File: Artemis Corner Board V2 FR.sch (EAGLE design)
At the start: 59 parts, among them U1 TPS562219, U2 TM4C1231C3PM, U21 LM1085IS, U3 TPS562219, U4 MCP2562FD

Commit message: Added Series Termination Resistors
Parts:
- added C25, C26: 12pF, rcl:C-USC0805
- added J1: (no value), FormE:CTI-20-MALE
- added R13: 1K, rcl:R-US_R0805
- added R14, R16, R17, R19: 22, rcl:R-US_R0805
- added Y1: NX3225GA, FormE:NX3225GA
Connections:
- removed net IR_SENSOR_1_ANALOG_OUT: H1.30, U2.PD0/AIN7/I2C3SCL/SSI1CLK/SSI3CLK/WT2CCP0
- removed net IR_SENSOR_1_DIGITAL_IN: H1.19, U2.PC2/T5CCP0/TDI
- removed net IR_SENSOR_1_DIGITAL_OUT: H1.15, U2.PC3/SWO/T5CCP1/TDO
- removed net IR_SENSOR_2_ANALOG_OUT: H1.29, U2.PD1/AIN6/I2C3SDA/SSI1FSS/SSI3FSS/WT2CCP1
- removed net IR_SENSOR_2_DIGITAL_IN: H1.18, U2.PC1/SWDIO/T4CCP1/TMS
- removed net IR_SENSOR_2_DIGITAL_OUT: H1.14, U2.PB3/I2C0SDA/T3CCP1
- removed net IR_SENSOR_3_ANALOG_OUT: H1.28, U2.PD2/AIN5/SSI1RX/SSI3RX/WT3CCP0
- removed net IR_SENSOR_3_DIGITAL_IN: H1.17, U2.PC0/SWCLK/T4CCP0/TCK
- removed net IR_SENSOR_3_DIGITAL_OUT: H1.13, U2.PB2/I2C0SCL/T3CCP0
- new net DAMPER_POS_OUT_TR: R16.2, U2.PA0/U0RX
- new net N$5: C25.1, U2.OSC1, Y1.P$1
- new net N$6: C26.1, U2.OSC0, Y1.P$3
- new net STRAIN_GADGE_VOLTMETER_IN_0_TR: R17.2, U2.PE3/AIN0
- new net STRAIN_GADGE_VOLTMETER_IN_1_TR: R19.2, U2.PE2/AIN1
- new net TCK: J1.11, R13.1, U2.PC0/SWCLK/T4CCP0/TCK
- new net TDI: J1.3
- new net TDO: J1.7, U2.PC2/T5CCP0/TDI, U2.PC3/SWO/T5CCP1/TDO
- new net TMS: J1.1, U2.PC1/SWDIO/T4CCP1/TMS
- new net TRCLK: U2.PF3/CAN0TX/SSI1FSS/T1CCP1/TRCLK
- new net WHEEL_SPEED_OUT_TR: R14.2, U2.PA4/SSI0RX
- net +12V: no longer H1.4, H1.5, H1.6
- net +3V3: now also J1.5
- net +5V: now also H1.10
- net DAMPER_POS_OUT: now also R16.1; no longer U2.PA0/U0RX
- net GND: now also C25.2, C26.2, H1.19, J1.10, J1.12, J1.16, J1.20, J1.4, J1.8, R13.2
- net MCU_RESET: now also J1.15
- net PROGRAMMING_CAN_N: now also H1.12
- net PROGRAMMING_CAN_P: now also H1.11
- net STRAIN_GADGE_VOLTMETER_IN_0: now also H1.28, R17.1; no longer H1.27, U2.PE3/AIN0
- net STRAIN_GADGE_VOLTMETER_IN_1: now also R19.1; no longer U2.PE2/AIN1
- net WHEEL_SPEED_OUT: now also R14.1; no longer U2.PA4/SSI0RX
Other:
- note added: "+5V to Image Sensor Board"
- note added: "Key"
- note added: "Manual Reset Button And JTAG Connector"
- note removed: "Manual Reset Button"

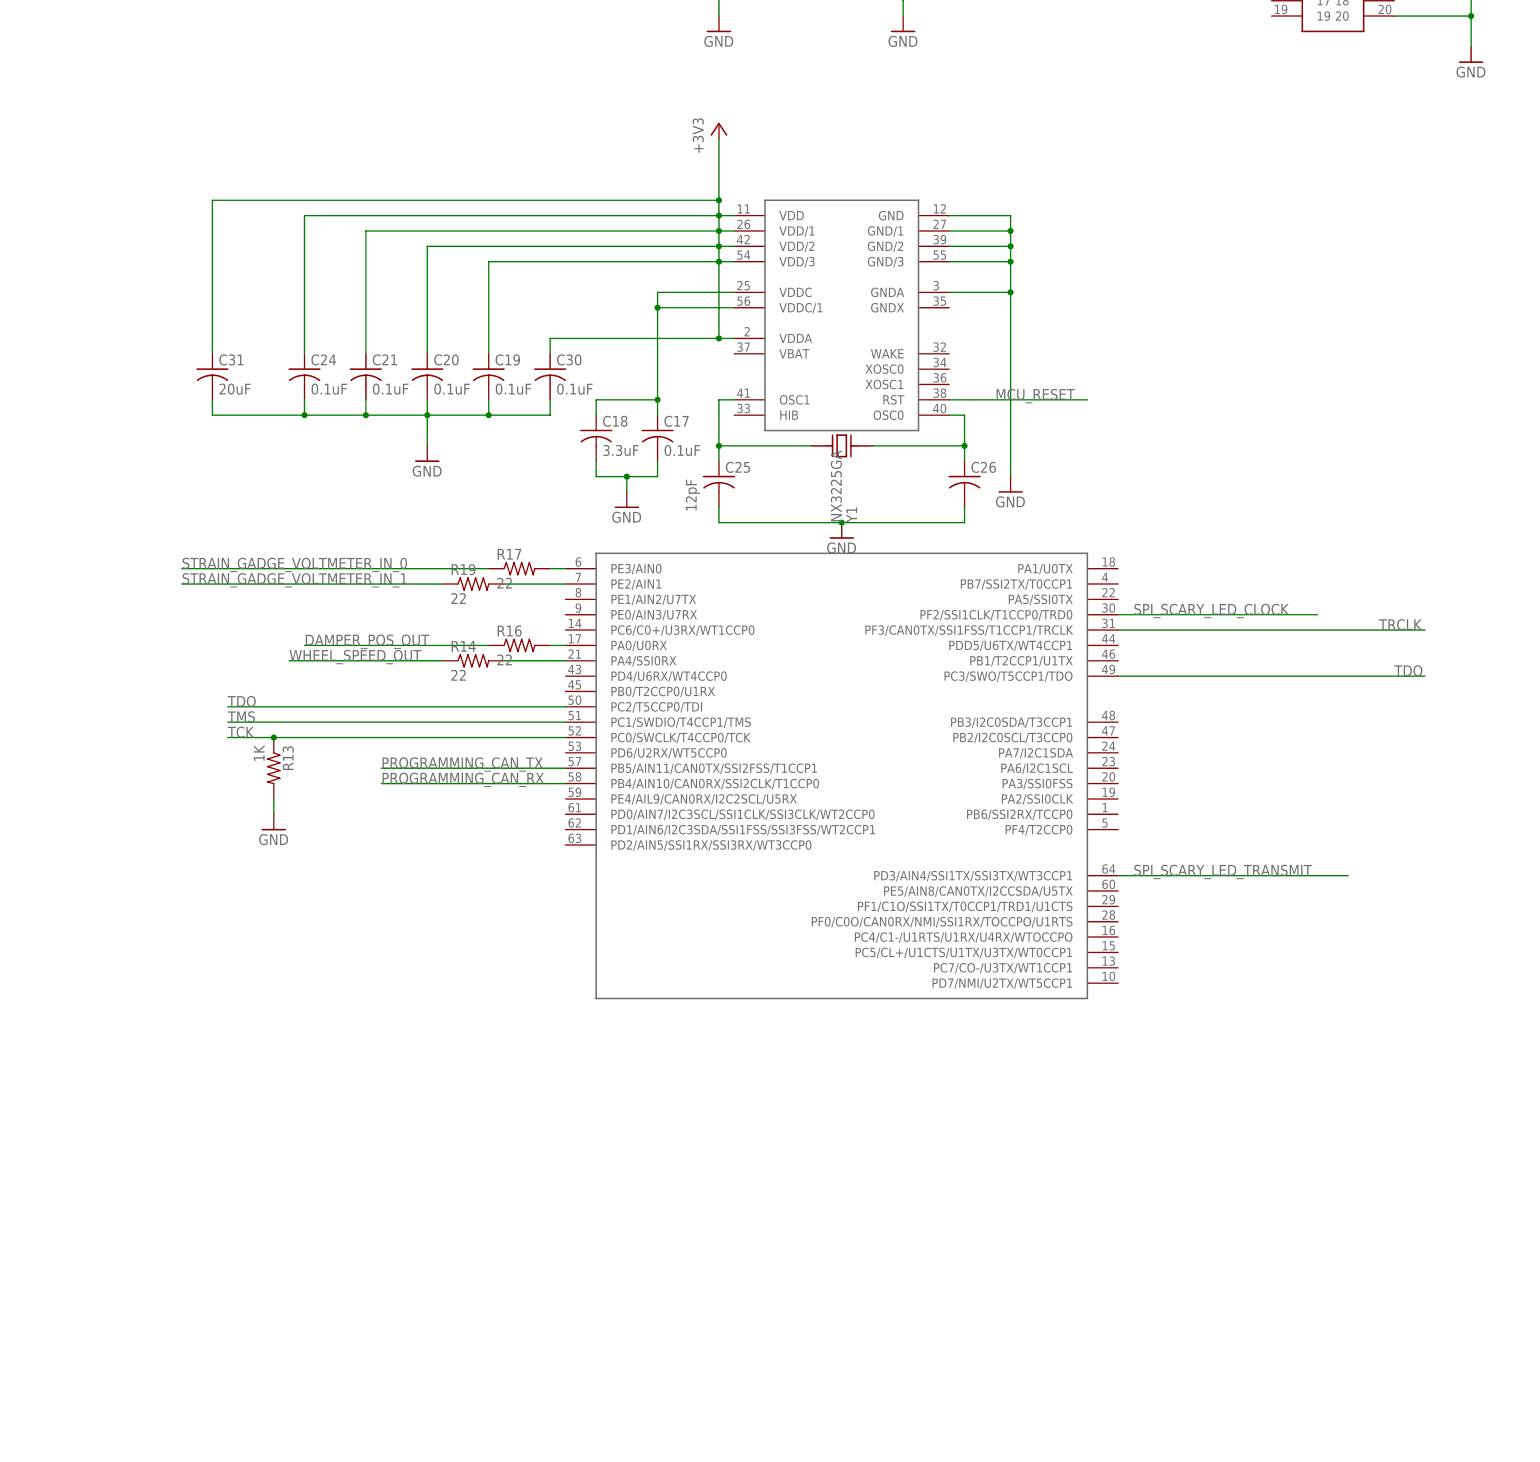
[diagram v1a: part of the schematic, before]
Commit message: fixed board errors and added ESD Protection
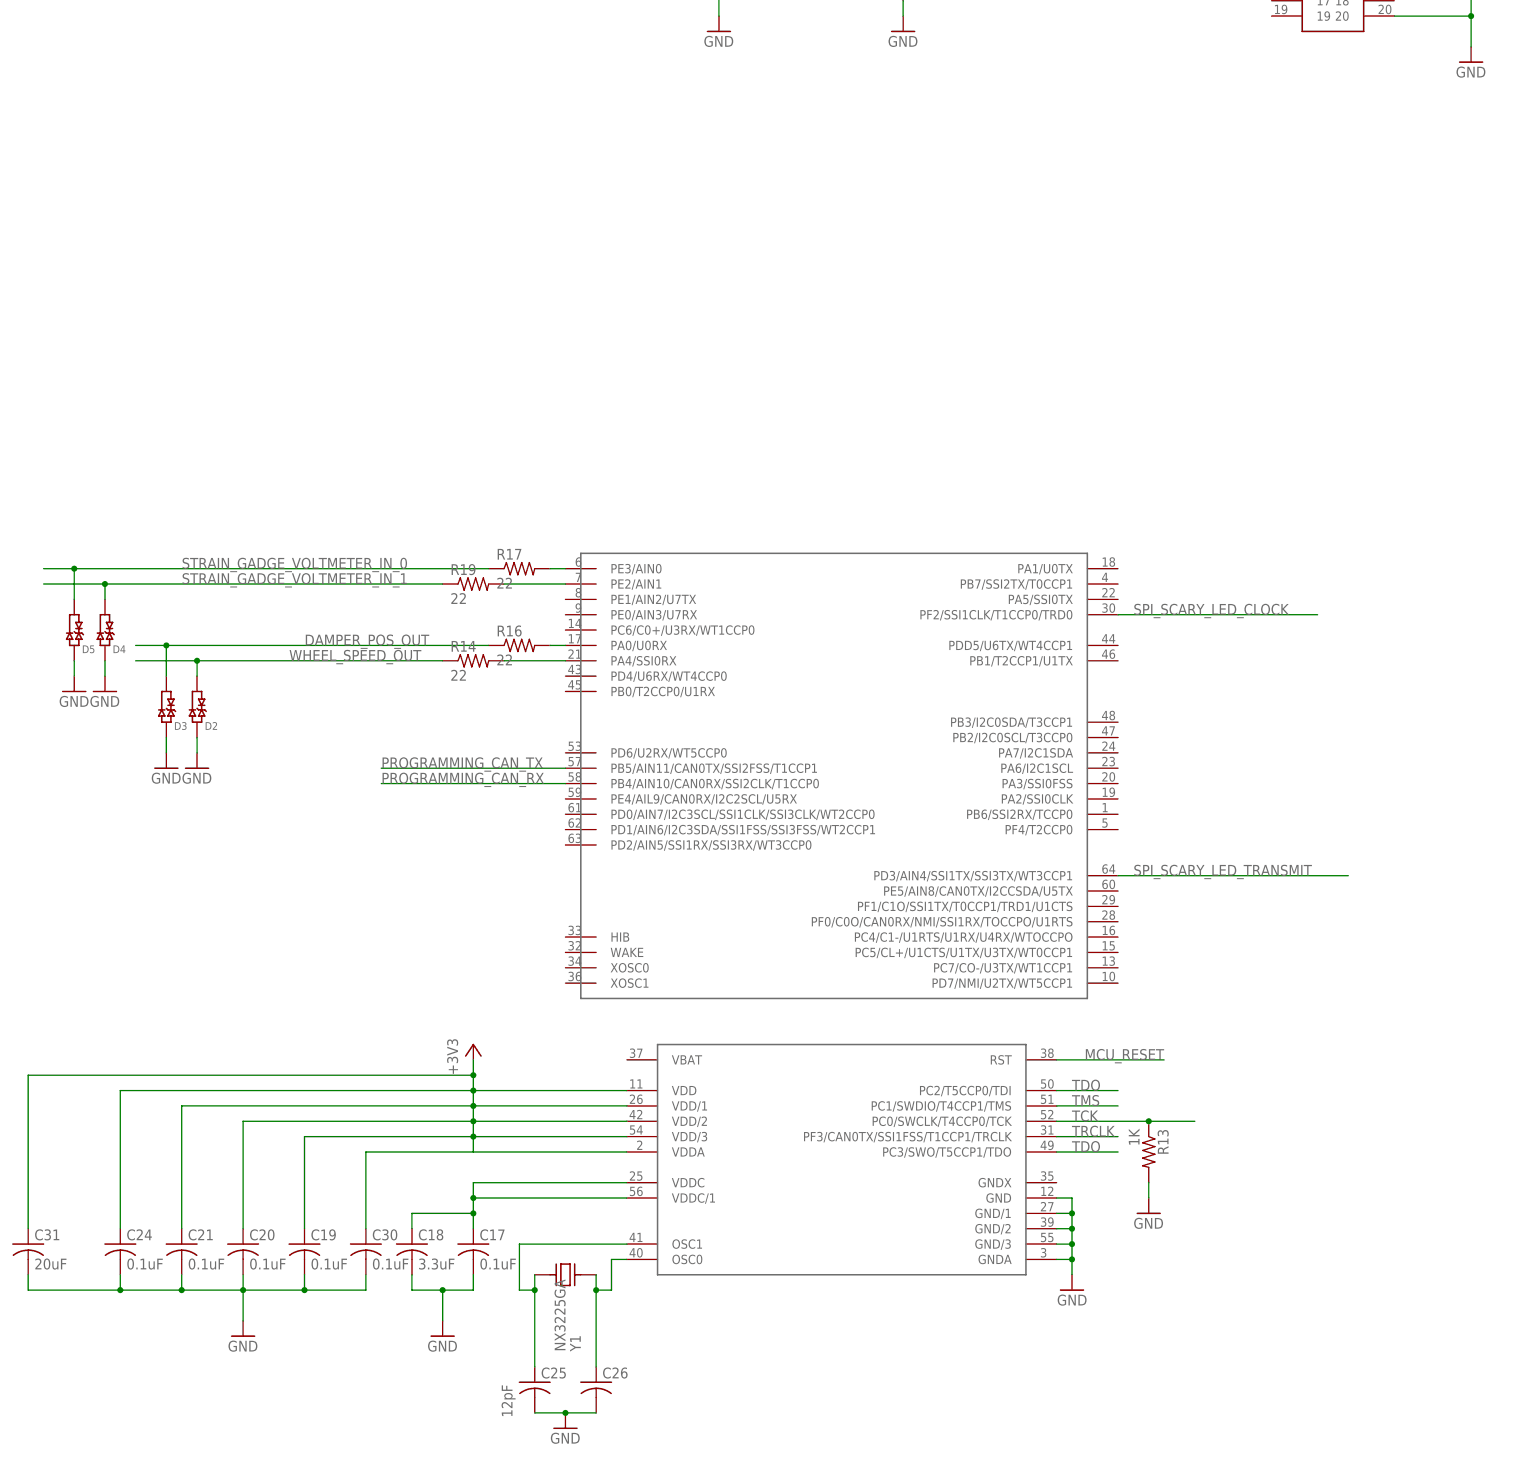
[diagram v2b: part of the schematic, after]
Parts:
- added D2, D3, D4, D5: TPD1E05U06, FormE:TPD1E05U06
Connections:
- net DAMPER_POS_OUT: now also D3.I/O
- net GND: now also D2.P$2, D3.P$2, D4.P$2, D5.P$2
- net STRAIN_GADGE_VOLTMETER_IN_0: now also D5.I/O
- net STRAIN_GADGE_VOLTMETER_IN_1: now also D4.I/O
- net WHEEL_SPEED_OUT: now also D2.I/O
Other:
- moved on the sheet: C17, C18, C19, C20, C21, C24, C25, C26, C30, C31, R13, Y1

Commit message: Made list fixes
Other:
- moved on the sheet: C1, C10, C11, C12, C13, C14, C15, C16, C17, C18, C19, C2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

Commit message: Updated a lot of stuff
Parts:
- added C62: 4.7uF, rcl:C-USC0805
- added C63: 0.1uF, rcl:C-USC0805
- added FB3: 220R @ 100M, launchpad:INDUCTOR
- added R20: 2K, rcl:R-US_R0805
- C31: value 20uF -> 22uF
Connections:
- net P$40 renamed VDDC
- net PROGRAMMING_CAN_N renamed CAN_N
- net PROGRAMMING_CAN_P renamed CAN_P
- net PROGRAMMING_CAN_RX renamed CAN_RX
- net PROGRAMMING_CAN_TX renamed CAN_TX
- new net FILTERED_+3V3: C19.1, C20.1, C21.1, C24.1, C30.1, C31.1, C62.1, C63.1, FB3.2, U2.VDD, U2.VDD/1, U2.VDD/2, U2.VDD/3, U2.VDDA
- new net N$7: R20.2, U2.OSC1
- net +3V3: now also FB3.1; no longer C19.1, C20.1, C21.1, C24.1, C30.1, C31.1, U2.VDD, U2.VDD/1, U2.VDD/2, U2.VDD/3, U2.VDDA
- net GND: now also C62.2, C63.2, U2.GNDX, U2.WAKE
- net N$5: now also R20.1; no longer U2.OSC1
- net TDI: now also U2.PC2/T5CCP0/TDI
- net TDO: no longer U2.PC2/T5CCP0/TDI
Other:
- moved on the sheet: C25, C26, Y1

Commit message: Changed to Tiva C with two CAN modules; modified sensor input scaling
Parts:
- removed C62: 4.7uF, rcl:C-USC0805
- removed C63: 0.1uF, rcl:C-USC0805
- removed C72, C73: 10uF, adafruit:C-USC0805
- removed D4, D5: TPD1E05U06, FormE:TPD1E05U06
- removed FB3: 220R @ 100M, launchpad:INDUCTOR
- removed LED5, LED6: GREEN, FormE:LEDCHIPLED_0805
- removed LED7: APA102C, FormE:APA102C
- removed S2: TE-FSM4JSMATR, FormE:TE-FSM4JSMATR
- removed U21: LM1085IS, FormE:LM1085
- added C27, C33, C34, C35: 0.1uF, rcl:C-USC0805
- added C28: 0.01uF, rcl:C-USC0805
- added C29: 1uF, rcl:C-USC0805
- added C32: 4.7uF, rcl:C-USC0805
- added C36, C42: 0.1uF, adafruit:C-USC0805
- added C37, C38: 10uF, adafruit:C-USC0805
- added C40: 2.2uF, rcl:C-USC0805
- added C41: 8200pF, adafruit:C-USC0805
- added C43, C44: 22uF, rcl:C-USC1210K
- added C45, C46, C47: 22uF, adafruit:C-USC0805
- added CF1, CF2, CF3, CF4: NFM21C, murata-filter:NFM21C
- added D1: TPD1E05U06, FormE:TPD1E05U06
- added IC1: FT232RL, ftdichip:FT232RL
- added JP1: (no value), pinhead:PINHD-1X2
- added JP2: (no value), FormE:USB_MICROB_PLUG-PTH3
- added L3: 4.7uH, FormE:SRP6540
- added Q1: BSS138, FormE:BSS138
- added R21: 1k, adafruit:R-US_R0805
- added R22: 54.9k, adafruit:R-US_R0805
- added R23: 10K, adafruit:R-US_R0805
- added R24: 1K, adafruit:R-US_R0805
- added S1: TE-FSM4JSMATR, FormE:TE-FSM4JSMATR
- added U5: MCP2562, FormE:MCP256X-SOIC
- added U6: TPS62177, FormE:TPS6217X
- added U7: TPS62175, FormE:TPS6217X
- added U8: TPS562219, FormE:TPS562219
- added Y2: 32.768kHz, FormE:AB26TRQ
- C1: value 0.1uF -> 100uF; device adafruit:C-USC0805 -> rcl:CPOL-USD/7343-31W; PARTNO GRM21BR71E104KA01L -> T494D107K010AT
- C10, C2: value 10uF -> 0.1uF; device adafruit:C-USC0805 -> rcl:C-USC0805; PARTNO GRM21BR61E106KA73L -> *
- C11: value 10uF -> 2.2uF; device adafruit:C-USC0805 -> rcl:C-USC0805; PARTNO GRM21BR61E106KA73L -> *
- C12: value 8200pF -> 2.2uF; device adafruit:C-USC0805 -> rcl:C-USC0805; PARTNO C0805C822K5RACTU -> *
- C13, C5: device adafruit:C-USC0805 -> rcl:C-USC0805
- C14, C16: value 22uF -> 0.1uF; device adafruit:C-USC0805 -> rcl:C-USC0805; PARTNO C2012JB1E226M125AC -> GRM21BR71E104KA01L
- C15: value 22uF -> DNP/0.1uF; device adafruit:C-USC0805 -> rcl:C-USC0805; PARTNO C2012JB1E226M125AC -> *
- C17, C30: PARTNO (none) -> GRM21BR71E104KA01L
- C18: value 3.3uF -> 22pF; PARTNO (none) -> C0805C220K5GACTU
- C19: value 0.1uF -> 1uF; PARTNO (none) -> *
- C20: value 0.1uF -> 22pF; PARTNO (none) -> C0805C220K5GACTU
- C21: value 0.1uF -> 2.2uF; PARTNO (none) -> *
- C22, C23: value 0.1uF -> 22pF; PARTNO GRM21BR71H104KA01L -> C0805C220K5GACTU
- C24: value 0.1uF -> 0.01uF; PARTNO (none) -> *
- C25: value 12pF -> 0.1uF; MPN 08051A150JAT2A -> (none); OC_NEWARK 96M1322 -> (none); PARTNO CL21C150JBANNNC -> GRM21BR71E104KA01L
- C26: value 12pF -> 0.01uF; MPN 08051A150JAT2A -> (none); OC_NEWARK 96M1322 -> (none); PARTNO CL21C150JBANNNC -> *
- C3: value 10uF -> 100pF; device adafruit:C-USC0805 -> rcl:C-USC0805; PARTNO GRM21BR61E106KA73L -> *
- C31: value 22uF -> 0.1uF; PARTNO (none) -> GRM21BR71E104KA01L
- C39: value 1uF -> 2.2uF; PARTNO EMK212B7105KG-T -> UMK212BB7225KG-T
- C4: value 8200pF -> 100pF; device adafruit:C-USC0805 -> rcl:C-USC0805; PARTNO C0805C822K5RACTU -> *
- C6, C7, C8: value 22uF -> 2.2uF; device adafruit:C-USC0805 -> rcl:C-USC0805; PARTNO C2012JB1E226M125AC -> *
- C9: value 0.1uF -> DNP; device adafruit:C-USC0805 -> rcl:C-USC0805; PARTNO GRM21BR71E104KA01L -> *
- D3: value TPD1E05U06 -> MM3Z3V3T1G; device FormE:TPD1E05U06 -> FormE:MM3Z3V3T1G; PARTNO (none) -> MM3Z3V3T1G
- L1, L2: value 4.7uH -> 10uH; PARTNO SRP6540-4R7M -> SRP6540-100M
- LED1, LED2: value APA102C -> ORANGE; device FormE:APA102C -> FormE:LEDCHIP-LED0805; PARTNO (none) -> 598-8130-107F
- LED3: device FormE:LEDCHIPLED_0805 -> FormE:LEDCHIP-LED0805
- LED4: value APA102C -> GREEN; device FormE:APA102C -> FormE:LEDCHIP-LED0805; PARTNO (none) -> 598-8170-107F
- R1: value 33.2K -> 100R; device adafruit:R-US_R0805 -> rcl:R-US_R0805; PARTNO ERA-6AEB5492V -> (none)
- R10: value 10K -> 270; device adafruit:R-US_R0805 -> rcl:R-US_R0805; PARTNO ERJ-6ENF1002V -> ERJ-6ENF2700V
- R11: value 100 -> 120R; PARTNO ERJ-6ENF1000V -> ERJ-6ENF1200V
- R12: value 2.2K -> 100R; PARTNO ERA-6AEB222V -> *
- R13: value 1K -> 10k; PARTNO ERA-6AEB222V -> *
- R14: value 22 -> 120R; PARTNO ERA-6AEB222V -> ERJ-6ENF1200V
- R15: value 0.007 -> 270; device adafruit:R-US_R0805 -> rcl:R-US_R0805; PARTNO PMR10EZPFU7L00 -> ERJ-6ENF2700V
- R16: value 22 -> 270; PARTNO ERA-6AEB222V -> ERJ-6ENF2700V
- R17: value 22 -> 10k; PARTNO ERA-6AEB222V -> ERJ-6ENF1002V
- R18: value 1K -> 4.7k; device adafruit:R-US_R0805 -> rcl:R-US_R0805; PARTNO ERJ-6ENF1001V -> ERJ-6ENF4701V
- R19: value 22 -> 75k; PARTNO ERA-6AEB222V -> ERJ-6ENF7502V
- R2: value 10K -> 100R; device adafruit:R-US_R0805 -> rcl:R-US_R0805; PARTNO ERJ-6ENF1002V -> (none)
- R20: value 2K -> 150k; PARTNO ERA-6AEB222V -> ERJ-6ENF1503V
- R3: value 10K -> 22; device adafruit:R-US_R0805 -> rcl:R-US_R0805; PARTNO ERJ-6ENF1002V -> *
- R4: value 1K -> 22; device adafruit:R-US_R0805 -> rcl:R-US_R0805; PARTNO ERJ-6ENF1001V -> *
- R5: value 33.2K -> 10k; device adafruit:R-US_R0805 -> rcl:R-US_R0805; PARTNO ERA-6AEB5492V -> ERJ-6ENF1002V
- R6: value 10K -> 10k; device adafruit:R-US_R0805 -> rcl:R-US_R0805
- R7: value 120/DNP -> 10k; PARTNO * -> ERJ-6ENF1002V
- R8: value 10K -> 39k; device adafruit:R-US_R0805 -> rcl:R-US_R0805; PARTNO ERJ-6ENF1002V -> ERJ-6ENF3902V
- R9: value 1K -> 75k; device adafruit:R-US_R0805 -> rcl:R-US_R0805; PARTNO ERJ-6ENF1001V -> ERJ-6ENF7502V
- U1: value TPS562219 -> OPA365AIDBVR; device FormE:TPS562219 -> FormE:OPA365AIDBV; PARTNO TPS562219DDFT -> (none)
- U2: value TM4C1231C3PM -> ADS1232IPWR; device FormE:TM4C1231C3PM -> FormE:ADS1232IPWR
- U3: value TPS562219 -> MCP2562; device FormE:TPS562219 -> FormE:MCP256X-SOIC; PARTNO TPS562219DDFT -> MCP2562FD-E/SN
- U4: value MCP2562FD -> TM4C123GH6PMI; device FormE:MCP256X-SOIC -> FormE:TM4C123GH6PM; PARTNO MCP2562FD-E/SN -> (none)
- Y1: value NX3225GA -> 16MHz; device FormE:NX3225GA -> FormE:CSM-3X; PARTNO (none) -> ECS-160-20-3X-TR
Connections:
- removed net +12V: H1.1, H1.2, H1.3, LED6.A, R10.2, R15.2
- removed net 12V_CURRENT_SENSE+: C73.1, R15.1, U21.OUT
- removed net CAN_N: H1.12, H1.35, R7.1, U4.CANL
- removed net CAN_P: H1.11, H1.34, R7.2, U4.CANH
- removed net CAN_RX: U2.PB4/AIN10/CAN0RX/SSI2CLK/T1CCP0, U4.RXD
- removed net CAN_TX: U2.PB5/AIN11/CAN0TX/SSI2FSS/T1CCP1, U4.TXD
- removed net DAMPER_POS_OUT: D3.I/O, H1.25, R16.1
- removed net DAMPER_POS_OUT_TR: R16.2, U2.PA0/U0RX
- removed net FILTERED_+3V3: C19.1, C20.1, C21.1, C24.1, C30.1, C31.1, C62.1, C63.1, FB3.2, U2.VDD, U2.VDD/1, U2.VDD/2, U2.VDD/3, U2.VDDA
- removed net MCU_RESET: C39.1, J1.15, R11.1, R12.2, U2.RST
- removed net N$11: LED6.C, R18.2
- removed net SPI_SCARY_LED_CLOCK: LED1.CI, U2.PF2/SSI1CLK/T1CCP0/TRD0
- removed net SPI_SCARY_LED_TRANSMIT: LED1.DI, U2.PD3/AIN4/SSI1TX/SSI3TX/WT3CCP1
- removed net SS_5V1: C4.1, U1.SS
- removed net SS_5V2: C12.1, U3.SS
- removed net STRAIN_GADGE_VOLTMETER_IN_0: D5.I/O, H1.28, R17.1
- removed net STRAIN_GADGE_VOLTMETER_IN_0_TR: R17.2, U2.PE3/AIN0
- removed net STRAIN_GADGE_VOLTMETER_IN_1: D4.I/O, H1.26, R19.1
- removed net STRAIN_GADGE_VOLTMETER_IN_1_TR: R19.2, U2.PE2/AIN1
- removed net SW_5V1: C5.2, L1.P$1, U1.SW
- removed net SW_5V2: C13.2, L2.P$1, U3.SW
- removed net TRCLK: U2.PF3/CAN0TX/SSI1FSS/T1CCP1/TRCLK
- removed net VBST_5V1: C5.1, U1.VBST
- removed net VBST_5V2: C13.1, U3.VBST
- removed net VDDC: C17.1, C18.1, U2.VDDC, U2.VDDC/1
- removed net VFB_5V1: R1.1, R2.2, U1.VFB
- removed net VFB_5V2: R5.1, R6.2, U3.VFB
- removed net WHEEL_SPEED_OUT: D2.I/O, H1.24, R10.1, R14.1
- removed net WHEEL_SPEED_OUT_TR: R14.2, U2.PA4/SSI0RX
- new net !RESET!: C15.1, J1.15, R12.2, R13.2, U4P.!RST!
- new net +1V2: C44.1, L2.P$2, R19.2, U7.SLEEP, U7.VOS
- new net ADC_!PWDN!: U2.!PDWN!, U4IO.PB1/T2CCP1/U1TX/USB0VBUS
- new net ADC_CHANNEL_SELECT: U2.A0, U4IO.PB3/I2C0SDA/T3CCP1
- new net ADC_GAIN_BIT_0: U2.GAIN0, U4IO.PB4/AIN10/CAN0RX/M0PWM2/SSI2CLK/T1CCP0
- new net ADC_GAIN_BIT_1: U2.GAIN1, U4IO.PB5/AIN11/CAN0TX/M0PWM3/SSI2FSS/T1CCP1
- new net ADC_MISO: U2.!DRDY!/DOUT, U4IO.PA4/SSI0RX
- new net ADC_SCLK: U2.SCLK, U4IO.PA2/SSI0CLK
- new net ADC_SPEED: U2.SPEED, U4IO.PB0/T2CCP0/U1RX/USB0ID
- new net ADC_TEMP_EN: U2.TEMP, U4IO.PB2/I2C0SCL/T3CCP0
- new net CAR_CAN_N: H1.35, R14.1, U5.CANL
- new net CAR_CAN_P: H1.34, R14.2, U5.CANH
- new net CAR_CAN_RX: U4IO.PE4/AIN9/CAN0RX/I2C2SCL/M0PWM4/M1PWM2/U5RX, U5.RXD
- new net CAR_CAN_TX: U4IO.PE5/AIN8/CAN0TX/I2C2SDA/M0PWM5/M1PWM3/U5TX, U5.TXD
- new net DAMPER_POSITION: D1.I/O, H1.25, R3.1
- new net DAMPER_POSITION_3V3: D3.CATHODE, R10.2, U4IO.PE3/AIN0
- new net FB_1V2: R19.1, R20.2, U7.FB
- new net IR_SENSOR_CAN_N: H1.12, R11.1, U3.CANL
- new net IR_SENSOR_CAN_P: H1.11, R11.2, U3.CANH
- new net N$14: R8.2, U1.INVERTING, U1.OUT
- new net N$17: C23.1, U4P.XOSC0, Y2.P$1
- new net N$19: JP1.2, U2.AINP2
- new net N$20: R3.2, R5.1, U1.NONINVERTING
- new net N$21: Q1.D, R4.2, R6.1
- new net N$22: C35.1, IC1.3V3OUT
- new net N$23: JP2.VCC, R18.1
- new net N$24: C22.2, C23.2, U4P.GNDX
- new net N$27: C2.1, C3.1, CF1.3, U2.AINP1
- new net N$29: C2.2, C4.1, CF2.1, U2.AINN1
- new net N$41: IC1.CBUS1, R16.1
- new net N$42: IC1.CBUS0, R15.1
- new net N$45: LED1.C, R15.2
- new net N$46: LED2.C, R16.2
- new net N$52: IC1.!RESET, R17.1, R18.2
- new net N$8: C10.2, U2.CAP1
- new net NTRST: J1.2
- new net PGOOD: U6.PG, U7.PG, U8.PGOOD
- new net RTCK: J1.9
- new net SENSOR_CAN_RX: U3.RXD, U4IO.PA0/CAN1RX/U0RX
- new net SENSOR_CAN_TX: U3.TXD, U4IO.PA1/CAN1TX/U0TX
- new net SS_5V: C41.1, U8.SS
- new net STRAIN_GAUGE_NEGATIVE: CF2.3, H1.26
- new net STRAIN_GAUGE_POSITIVE: CF1.1, H1.28
- new net SW_1V2: L2.P$1, U7.SW
- new net SW_3V3: L1.P$1, U6.SW
- new net SW_5V: C42.2, L3.P$1, U8.SW
- new net UART_RX: IC1.TXD, U4IO.PC4/C1-/IDX1/M0PWM6/U1RTS/U1RX/U4RX/WT0CCP0
- new net UART_TX: IC1.RXD, U4IO.PC5/C1+/M0PWM7/PHA1/U1CTS/U1TX/U4TX/WT0CCP1
- new net USB_D_N: IC1.USBDM, JP2.D-
- new net USB_D_P: IC1.USBDP, JP2.D+
- new net VBST_5V: C42.1, U8.VBST
- new net VFB_5V: R22.1, R23.2, U8.VFB
- new net WHEEL_TACHOMETER: D2.I/O, H1.24, R4.1
- new net WHEEL_TACHOMETER_3V3: Q1.S, R7.1, U4IO.PB6/M0PWM0/SSI2RX/T0CCP0
- net +3V3: now also C12.1, C13.1, C24.1, C25.1, C26.1, C27.1, C28.1, C29.1, C31.1, C34.1, C43.1, IC1.VCCIO, LED1.A, LED2.A, LED3.A, Q1.G, R13.1, R7.2, U2.DVDD, U3.SPLIT/VIO, U4P.VBAT, U4P.VDD, U4P.VDDA, U5.SPLIT/VIO, U6.SLEEP, U6.VOS; no longer C23.1, C6.1, C7.1, C8.1, FB3.1, LED5.A, R1.2, R12.1, U4.SPLIT/VIO
- net +5V: now also C11.1, C30.1, C32.1, C33.1, C45.1, C46.1, C47.1, C5.1, IC1.VCC, L3.P$2, LED4.A, R1.1, R22.2, R6.2, U1.V+, U2.AVDD, U3.VDD, U5.VDD; no longer C15.1, C16.1, C22.1, H1.10, L2.P$2, LED1.+5V, LED2.+5V, LED3.A, LED4.+5V, LED7.+5V, R5.2, U4.VDD
- net GND: now also C13.2, C27.2, C28.2, C29.2, C32.2, C33.2, C34.2, C35.2, C36.2, C37.2, C38.2, C40.2, C41.2, C43.2, C44.2, C45.2, C46.2, C47.2, C5.2, CF1.2@1, CF2.2@1, CF3.2@1, CF4.2@1, D1.P$2, D3.ANODE, IC1.GND, IC1.GND@1, IC1.GND@2, IC1.GND@A, IC1.TEST, JP2.GND, JP2.SHIELD, R17.2, R20.1, R21.1, R23.1, R24.1, R5.2, S1.3, S1.4, U1.V-, U2.AGND, U2.CLKIN/XTAL1, U2.DGND, U3.STBY, U3.VSS, U4P.!WAKE!, U4P.GND, U4P.GNDA, U5.STBY, U5.VSS, U6.AGND, U6.FB, U6.NC, U6.PGND, U7.AGND, U7.NC, U7.PGND, U8.GND; no longer C1.2, C10.2, C2.2, C22.2, C23.2, C6.2, C62.2, C63.2, C72.2, C73.2, D3.P$2, D4.P$2, D5.P$2, H1.19, H1.20, H1.21, H1.22, H1.23, LED1.GND, LED2.GND, LED4.GND, LED7.GND, R13.2, R18.1, R4.1, R6.1, S2.3, S2.4, U1.GND, U2.GND, U2.GND/1, U2.GND/2, U2.GND/3, U2.GNDA, U2.GNDX, U2.WAKE, U21.ADJ, U3.GND, U4.STBY, U4.VSS
- net N$1: now also C18.1, U4P.OSC1, Y1.P$1; no longer LED1.DO, LED2.DI
- net N$10: now also C6.1, C7.1, CF3.3, U2.REFP; no longer LED2.DO, LED4.DI
- net N$12: now also C6.2, C8.1, CF4.1, U2.REFN; no longer LED4.CO, LED7.CI
- net N$13: now also C1.+, CF3.1, R1.2; no longer LED4.DO, LED7.DI
- net N$15: now also C22.1, U4P.XOSC1, Y2.P$3; no longer LED2.CO, LED4.CI
- net N$16: now also C9.1, R10.1, R8.1, R9.2; no longer LED1.CO, LED2.CI
- net N$18: now also C1.-, CF4.3, R2.2; no longer R11.2, S2.1, S2.2
- net N$2: now also LED3.C, R21.2; no longer LED5.C, R4.2
- net N$3: now also LED4.C, R24.2; no longer LED3.C, R9.2
- net N$4: now also C20.1, U4P.OSC0, Y1.P$3; no longer R8.2, U3.EN
- net N$5: now also C10.1, U2.CAP2; no longer C25.1, R20.1, Y1.P$1
- net N$6: now also C16.1, C17.1, C19.1, C21.1, U4P.VDDC; no longer C26.1, U2.OSC0, Y1.P$3
- net N$7: now also R12.1, S1.1, S1.2; no longer R20.2, U2.OSC1
- net N$9: now also JP1.1, U2.AINN2; no longer R3.2, U1.EN
- net TCK: now also U4IO.PC0/SWCLK/T4CCP0/TCK; no longer R13.1, U2.PC0/SWCLK/T4CCP0/TCK
- net TDI: now also U4IO.PC2/T5CCP0/TDI; no longer U2.PC2/T5CCP0/TDI
- net TDO: now also U4IO.PC3/SWO/T5CCP1/TDO; no longer U2.PC3/SWO/T5CCP1/TDO
- net TMS: now also U4IO.PC1/SWDIO/T4CCP1/TMS; no longer U2.PC1/SWDIO/T4CCP1/TMS
- net VCC: now also C36.1, C37.1, C38.1, C39.1, C40.1, U6.EN, U6.VIN, U7.EN, U7.VIN, U8.EN, U8.VIN; no longer C1.1, C10.1, C11.1, C2.1, C3.1, C72.1, C9.1, H1.32, R3.1, R8.1, U1.VIN, U21.IN, U3.VIN
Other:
- note added: "+1v2 buck"
- note added: "+3v3 buck"
- note added: "Damper 5V"
- note added: "Damper GND"
- note added: "GAIN: 00 : gain=1 01 : gain=2 10 : gain=64 11 : gain=128 SPEED HIGH: 80 samples/second LOW: 10 samples/second !PWDN! HIGH: ADC is on LOW: ADC is off TEMP HIGH: disconnect AIN1/2 and connect temperature sensors LOW: connect AIN1/2 and disconnect temperature sensors A0 HIGH: use AIN2 LOW: use AIN1"
- note added: "GLV battery GND"
- note added: "GLV battery VCC"
- note added: "Hall Effect Sensor: Texense RS-M10 WS http://www.sens4speed.com/en/products/wheel-speed/rs-m10ws_3.html"
- note added: "IR Camera: Flir Lepton 500-0659-01 http://www.digikey.com/product-detail/en/500-0659-01/500-0659-01-ND/5215153"
- note added: "KEY"
- note added: "NC"
- note added: "RX"
- note added: "SRP6540-100M"
- note added: "See TI's reference design: ADS1232REF Also read: http://www.ti.com/lit/ml/slyp163/slyp163.pdf"
- note added: "Shock Potentiometer: Texense RSL 75mm http://www.sens4speed.com/en/products/potentiometers/rsl-75mm_14.html"
- note added: "Strain Gauge 5V"
- note added: "Strain Gauge GND"
- note added: "Strain Gauge: Micro-Measurements MMF003129 (125UN series) http://www.digikey.com/product-detail/en/CEA-06-125UN-350/1033-1004-ND/2503695 Requires 3 additional 350-ohm precision resistors to form a wheatstone bridge"
- note added: "TX"
- note added: "Tire Temperature 5V"
- note added: "Tire Temperature GND"
- note added: "USB Cannot provide Power"
- note added: "Wheel Speed 5V"
- note added: "Wheel Speed GND"
- note removed: "+5V to Image Sensor Board"
- note removed: "25V or higher caps"
- note removed: "<-- R1 <-- R2"
- note removed: "ARTEMIS CORNER BOARD V2 FR"
- note removed: "AUX BATTERY VIN = 4.5 - 17 V"
- note removed: "CAN CONECTION"
- note removed: "General IO for CAN? PWM?"
- note removed: "Key"
- note removed: "LEDs that serve no practical function, exept to look "Sick as fuck""
- note removed: "Manual Reset Button And JTAG Connector"
- note removed: "REGULATED OUTPUT"
- note removed: "SWITCHING FREQUENCY 650kHz"
- note removed: "Scary LEDs"
- note removed: "To enable differential sampling, software must set the Dn bit in the ADCSSCTL0n register in a step's configuration nibble. TM4C1231C3PM 774"
- note removed: "Voltage Regulators"
- note removed: "Vout = .765*(1+(R1/R2)) VOUT | R1 -------|--------- 5.0V | 54.9K 3.3V | 33.2K 2.8V | 26.1K 1.8V | 13.7K 1.2V | 5.76K"
- moved on the sheet: C10, C11, C12, C13, C14, C15, C16, C17, C18, C19, C2, C20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
